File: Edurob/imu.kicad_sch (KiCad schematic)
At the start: 9 parts

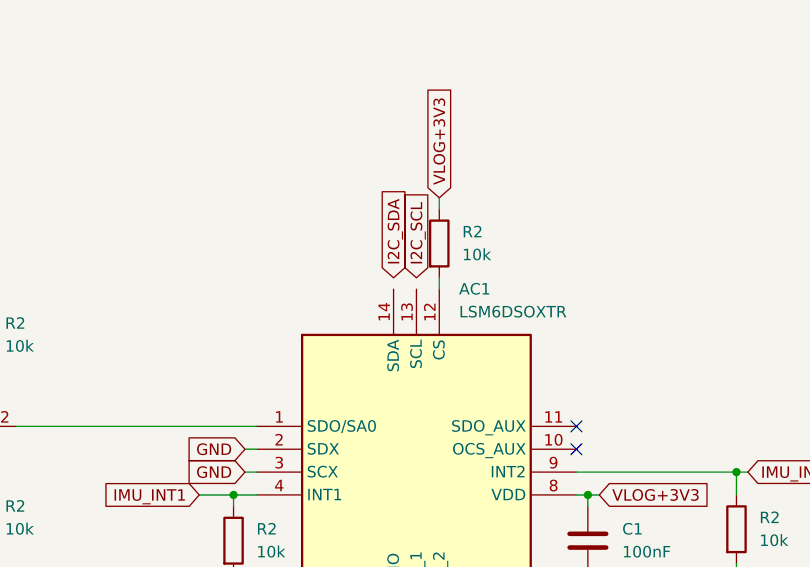
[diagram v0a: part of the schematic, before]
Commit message: Added GPIO Expander, finalized Connector positions
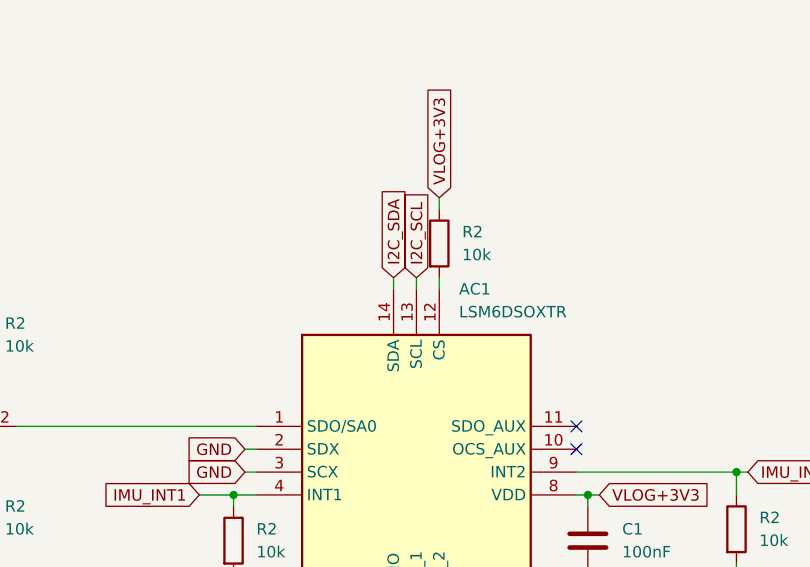
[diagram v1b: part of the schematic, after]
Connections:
- net I2C_SCL: now also AC1.13 (SCL)
- net I2C_SDA: now also AC1.14 (SDA)
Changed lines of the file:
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@@
+    (stroke (width 0) (type default))
+  )
+  (wire (pts (xy 142.24 59.69) (xy 142.24 60.96))
     (stroke (width 0) (type default))
   )
@@
   )
   (wire (pts (xy 118.11 83.82) (xy 121.92 83.82))
+    (stroke (width 0) (type default))
+  )
+  (wire (pts (xy 139.7 59.69) (xy 139.7 60.96))
     (stroke (width 0) (type default))
   )
@@
       )
       (project "Edurob"
-        (path "/ea495553-3cd2-4380-af57-b7ab16ec3dc9/89de68d6-46a2-4637-9552-cf7ed3825f2a"
-          (reference "C9") (unit 1)
-        )
         (path "/ea495553-3cd2-4380-af57-b7ab16ec3dc9/172d60ec-c5c3-4534-881f-0378b6cc8d8f"
           (reference "C10") (unit 1)
@@
       )
       (project "Edurob"
-        (path "/ea495553-3cd2-4380-af57-b7ab16ec3dc9"
-          (reference "R1") (unit 1)
-        )
-        (path "/ea495553-3cd2-4380-af57-b7ab16ec3dc9/8aa2f8b0-d8d3-42d6-a936-678d5127e1c2"
-          (reference "R4") (unit 1)
-        )
         (path "/ea495553-3cd2-4380-af57-b7ab16ec3dc9/172d60ec-c5c3-4534-881f-0378b6cc8d8f"
           (reference "R11") (unit 1)
@@
       )
       (project "Edurob"
-        (path "/ea495553-3cd2-4380-af57-b7ab16ec3dc9"
-          (reference "R1") (unit 1)
-        )
-        (path "/ea495553-3cd2-4380-af57-b7ab16ec3dc9/8aa2f8b0-d8d3-42d6-a936-678d5127e1c2"
-          (reference "R4") (unit 1)
-        )
         (path "/ea495553-3cd2-4380-af57-b7ab16ec3dc9/172d60ec-c5c3-4534-881f-0378b6cc8d8f"
           (reference "R6") (unit 1)
@@
       )
       (project "Edurob"
-        (path "/ea495553-3cd2-4380-af57-b7ab16ec3dc9"
-          (reference "R1") (unit 1)
-        )
-        (path "/ea495553-3cd2-4380-af57-b7ab16ec3dc9/8aa2f8b0-d8d3-42d6-a936-678d5127e1c2"
-          (reference "R4") (unit 1)
-        )
         (path "/ea495553-3cd2-4380-af57-b7ab16ec3dc9/172d60ec-c5c3-4534-881f-0378b6cc8d8f"
           (reference "R5") (unit 1)
@@
       )
       (project "Edurob"
-        (path "/ea495553-3cd2-4380-af57-b7ab16ec3dc9"
-          (reference "R1") (unit 1)
-        )
-        (path "/ea495553-3cd2-4380-af57-b7ab16ec3dc9/8aa2f8b0-d8d3-42d6-a936-678d5127e1c2"
-          (reference "R4") (unit 1)
-        )
         (path "/ea495553-3cd2-4380-af57-b7ab16ec3dc9/172d60ec-c5c3-4534-881f-0378b6cc8d8f"
           (reference "R33") (unit 1)
@@
       )
       (project "Edurob"
-        (path "/ea495553-3cd2-4380-af57-b7ab16ec3dc9"
-          (reference "R1") (unit 1)
-        )
-        (path "/ea495553-3cd2-4380-af57-b7ab16ec3dc9/8aa2f8b0-d8d3-42d6-a936-678d5127e1c2"
-          (reference "R4") (unit 1)
-        )
         (path "/ea495553-3cd2-4380-af57-b7ab16ec3dc9/172d60ec-c5c3-4534-881f-0378b6cc8d8f"
           (reference "R10") (unit 1)
@@
       )
       (project "Edurob"
-        (path "/ea495553-3cd2-4380-af57-b7ab16ec3dc9/89de68d6-46a2-4637-9552-cf7ed3825f2a"
-          (reference "C9") (unit 1)
-        )
         (path "/ea495553-3cd2-4380-af57-b7ab16ec3dc9/172d60ec-c5c3-4534-881f-0378b6cc8d8f"
           (reference "C11") (unit 1)

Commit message: Release v1.0.1
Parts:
- AC1: Mouser Price/Stock https://www.mouser.co.uk/ProductDetail/STMicroelectronics/L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 -> https://www.mouser.de/ProductDetail/511-LSM6DSOXTR; Placed (none) -> True
- C1: Manufacturer_Name (none) -> KYOCERA AVX; Manufacturer_Part_Number (none) -> KGM15BR71E104KT; Mouser Part Number (none) -> 581-KGM15BR71E104KT; Mouser Price/Stock (none) -> https://www.mouser.de/ProductDetail/581-KGM15BR71E104KT; Placed (none) -> True
- JP1: Placed (none) -> False
- R2: value 10k -> 10K; Manufacturer_Name (none) -> Vishay / Dale; Manufacturer_Part_Number (none) -> CRCW060310K0FKEA; Mouser Part Number (none) -> 71-CRCW0603-10K-E3; Mouser Price/Stock (none) -> https://www.mouser.de/ProductDetail/71-CRCW0603-10K-E3; Placed (none) -> True
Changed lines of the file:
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@@
+      (effects (font (size 1.27 1.27)) hide)
+    )
+    (property "Manufacturer_Name" "KYOCERA AVX" (at 128.27 109.22 0)
+      (effects (font (size 1.27 1.27)) hide)
+    )
+    (property "Manufacturer_Part_Number" "KGM15BR71E104KT" (at 128.27 109.22 0)
+      (effects (font (size 1.27 1.27)) hide)
+    )
+    (property "Mouser Part Number" "581-KGM15BR71E104KT" (at 128.27 109.22 0)
+      (effects (font (size 1.27 1.27)) hide)
+    )
+    (property "Mouser Price/Stock" "https://www.mouser.de/ProductDetail/581-KGM15BR71E104KT" (at 128.27 109.22 0)
+      (effects (font (size 1.27 1.27)) hide)
+    )
+    (property "Placed" "True" (at 128.27 109.22 0)
       (effects (font (size 1.27 1.27)) hide)
     )
@@
       (effects (font (size 1.27 1.27)) hide)
     )
+    (property "Placed" "False" (at 93.98 76.2 0)
+      (effects (font (size 1.27 1.27)) hide)
+    )
     (pin "3")
     (pin "1")
@@
       (effects (font (size 1.27 1.27)) (justify left))
     )
-    (property "Value" "10k" (at 124.46 90.1699 0)
+    (property "Value" "10K" (at 124.46 90.1699 0)
       (effects (font (size 1.27 1.27)) (justify left))
     )
@@
       (effects (font (size 1.27 1.27)) hide)
     )
+    (property "Manufacturer_Name" "Vishay / Dale" (at 121.92 88.9 0)
+      (effects (font (size 1.27 1.27)) hide)
+    )
+    (property "Manufacturer_Part_Number" "CRCW060310K0FKEA" (at 121.92 88.9 0)
+      (effects (font (size 1.27 1.27)) hide)
+    )
+    (property "Mouser Part Number" "71-CRCW0603-10K-E3" (at 121.92 88.9 0)
+      (effects (font (size 1.27 1.27)) hide)
+    )
+    (property "Mouser Price/Stock" "https://www.mouser.de/ProductDetail/71-CRCW0603-10K-E3" (at 121.92 88.9 0)
+      (effects (font (size 1.27 1.27)) hide)
+    )
+    (property "Placed" "True" (at 121.92 88.9 0)
+      (effects (font (size 1.27 1.27)) hide)
+    )
     (pin "1")
     (pin "2")
@@
       (effects (font (size 1.27 1.27)) (justify left))
     )
-    (property "Value" "10k" (at 96.52 67.3099 0)
+    (property "Value" "10K" (at 96.52 67.3099 0)
       (effects (font (size 1.27 1.27)) (justify left))
     )
@@
       (effects (font (size 1.27 1.27)) hide)
     )
+    (property "Manufacturer_Name" "Vishay / Dale" (at 93.98 66.04 0)
+      (effects (font (size 1.27 1.27)) hide)
+    )
+    (property "Manufacturer_Part_Number" "CRCW060310K0FKEA" (at 93.98 66.04 0)
+      (effects (font (size 1.27 1.27)) hide)
+    )
+    (property "Mouser Part Number" "71-CRCW0603-10K-E3" (at 93.98 66.04 0)
+      (effects (font (size 1.27 1.27)) hide)
+    )
+    (property "Mouser Price/Stock" "https://www.mouser.de/ProductDetail/71-CRCW0603-10K-E3" (at 93.98 66.04 0)
+      (effects (font (size 1.27 1.27)) hide)
+    )
+    (property "Placed" "True" (at 93.98 66.04 0)
+      (effects (font (size 1.27 1.27)) hide)
+    )
     (pin "1")
     (pin "2")
@@
       (effects (font (size 1.27 1.27)) (justify left top) hide)
     )
-    (property "Height" "" (at 156.21 463.5 0)
-      (effects (font (size 1.27 1.27)) (justify left top) hide)
-    )
     (property "Mouser Part Number" "511-LSM6DSOXTR" (at 156.21 563.5 0)
       (effects (font (size 1.27 1.27)) (justify left top) hide)
     )
-    (property "Mouser Price/Stock" "https://www.mouser.co.uk/ProductDetail/STMicroelectronics/LSM6DSOXTR?qs=l7cgNqFNU1i9dcjzItLpVQ%3D%3D" (at 156.21 663.5 0)
+    (property "Mouser Price/Stock" "https://www.mouser.de/ProductDetail/511-LSM6DSOXTR" (at 156.21 663.5 0)
       (effects (font (size 1.27 1.27)) (justify left top) hide)
     )
@@
     (property "Manufacturer_Part_Number" "LSM6DSOXTR" (at 156.21 863.5 0)
       (effects (font (size 1.27 1.27)) (justify left top) hide)
+    )
+    (property "Placed" "True" (at 124.46 76.2 0)
+      (effects (font (size 1.27 1.27)) hide)
     )
     (pin "13")
@@
       (effects (font (size 1.27 1.27)) (justify left))
     )
-    (property "Value" "10k" (at 96.52 87.6299 0)
+    (property "Value" "10K" (at 96.52 87.6299 0)
       (effects (font (size 1.27 1.27)) (justify left))
     )
@@
       (effects (font (size 1.27 1.27)) hide)
     )
+    (property "Manufacturer_Name" "Vishay / Dale" (at 93.98 86.36 0)
+      (effects (font (size 1.27 1.27)) hide)
+    )
+    (property "Manufacturer_Part_Number" "CRCW060310K0FKEA" (at 93.98 86.36 0)
+      (effects (font (size 1.27 1.27)) hide)
+    )
+    (property "Mouser Part Number" "71-CRCW0603-10K-E3" (at 93.98 86.36 0)
+      (effects (font (size 1.27 1.27)) hide)
+    )
+    (property "Mouser Price/Stock" "https://www.mouser.de/ProductDetail/71-CRCW0603-10K-E3" (at 93.98 86.36 0)
+      (effects (font (size 1.27 1.27)) hide)
+    )
+    (property "Placed" "True" (at 93.98 86.36 0)
+      (effects (font (size 1.27 1.27)) hide)
+    )
     (pin "1")
     (pin "2")
@@
       (effects (font (size 1.27 1.27)) (justify left))
     )
-    (property "Value" "10k" (at 180.34 88.8999 0)
+    (property "Value" "10K" (at 180.34 88.8999 0)
       (effects (font (size 1.27 1.27)) (justify left))
     )
@@
       (effects (font (size 1.27 1.27)) hide)
     )
+    (property "Manufacturer_Name" "Vishay / Dale" (at 177.8 87.63 0)
+      (effects (font (size 1.27 1.27)) hide)
+    )
+    (property "Manufacturer_Part_Number" "CRCW060310K0FKEA" (at 177.8 87.63 0)
+      (effects (font (size 1.27 1.27)) hide)
+    )
+    (property "Mouser Part Number" "71-CRCW0603-10K-E3" (at 177.8 87.63 0)
+      (effects (font (size 1.27 1.27)) hide)
+    )
+    (property "Mouser Price/Stock" "https://www.mouser.de/ProductDetail/71-CRCW0603-10K-E3" (at 177.8 87.63 0)
+      (effects (font (size 1.27 1.27)) hide)
+    )
+    (property "Placed" "True" (at 177.8 87.63 0)
+      (effects (font (size 1.27 1.27)) hide)
+    )
     (pin "1")
     (pin "2")
@@
       (effects (font (size 1.27 1.27)) (justify left))
     )
-    (property "Value" "10k" (at 147.32 57.1499 0)
+    (property "Value" "10K" (at 147.32 57.1499 0)
       (effects (font (size 1.27 1.27)) (justify left))
     )
@@
       (effects (font (size 1.27 1.27)) hide)
     )
+    (property "Manufacturer_Name" "Vishay / Dale" (at 144.78 55.88 0)
+      (effects (font (size 1.27 1.27)) hide)
+    )
+    (property "Manufacturer_Part_Number" "CRCW060310K0FKEA" (at 144.78 55.88 0)
+      (effects (font (size 1.27 1.27)) hide)
+    )
+    (property "Mouser Part Number" "71-CRCW0603-10K-E3" (at 144.78 55.88 0)
+      (effects (font (size 1.27 1.27)) hide)
+    )
+    (property "Mouser Price/Stock" "https://www.mouser.de/ProductDetail/71-CRCW0603-10K-E3" (at 144.78 55.88 0)
+      (effects (font (size 1.27 1.27)) hide)
+    )
+    (property "Placed" "True" (at 144.78 55.88 0)
+      (effects (font (size 1.27 1.27)) hide)
+    )
     (pin "1")
     (pin "2")
@@
       (effects (font (size 1.27 1.27)) hide)
     )
+    (property "Manufacturer_Name" "KYOCERA AVX" (at 161.29 88.9 0)
+      (effects (font (size 1.27 1.27)) hide)
+    )
+    (property "Manufacturer_Part_Number" "KGM15BR71E104KT" (at 161.29 88.9 0)
+      (effects (font (size 1.27 1.27)) hide)
+    )
+    (property "Mouser Part Number" "581-KGM15BR71E104KT" (at 161.29 88.9 0)
+      (effects (font (size 1.27 1.27)) hide)
+    )
+    (property "Mouser Price/Stock" "https://www.mouser.de/ProductDetail/581-KGM15BR71E104KT" (at 161.29 88.9 0)
+      (effects (font (size 1.27 1.27)) hide)
+    )
+    (property "Placed" "True" (at 161.29 88.9 0)
+      (effects (font (size 1.27 1.27)) hide)
+    )
